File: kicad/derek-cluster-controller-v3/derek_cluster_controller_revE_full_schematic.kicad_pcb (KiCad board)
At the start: 6 copper layers, 220 x 220 mm, 59 parts, among them J1 XY301V_5.08_2P_5V_INPUT_15A, J2 FMHXG_RJ45NMCCFC_90D_RIGHT_AN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, J26 ADAFRUIT_815_PCA9685_BREAKOUT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, J3 FMHXG_RJ45NMCCFC_90D_RIGHT_AN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, J31 JST_XH_3PIN_PIR_LEFT, J32 JST_XH_3PIN_PIR_CENTER, J33 JST_XH_3PIN_PIR_RIGHT, J4 FMHXG_RJ45NMCCFC_90D_RIGHT_AN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, J40 TEST_POWER_3PIN, J41 TEST_I2C_4PIN, J42 TEST_LED_3PIN, J5 FMHXG_RJ45NMCCFC_90D_RIGHT_AN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, J51 DF1_SPEAKER_2PIN, J52 DF2_SPEAKER_2PIN, J6 FMHXG_RJ45NMCCFC_90D_RIGHT_AN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, J61 DF1_DAC_LR_GND_3PIN, J62 DF2_DAC_LR_GND_3PIN, J7 FMHXG_RJ45NMCCFC_90D_RIGHT_AN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, J8 FMHXG_RJ45NMCCFC_90D_RIGHT_AN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, J9 FMHXG_RJ45NMCCFC_90D_RIGHT_AN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, Q1 D2PAK_PMOS_REVERSE_PROTECTION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, SW1 DIP_SWITCH_4_SPST_2p54_CLUSTE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, U1 ESP32_S3_DEVKITC_1_SOCKET_2x1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, U3 DFPLAYER_MINI_STANDARD_20x20_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, U4 DFPLAYER_MINI_STANDARD_20x20_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, U5 SN74AHCT125N_DIP14_OR_SMD_LEV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

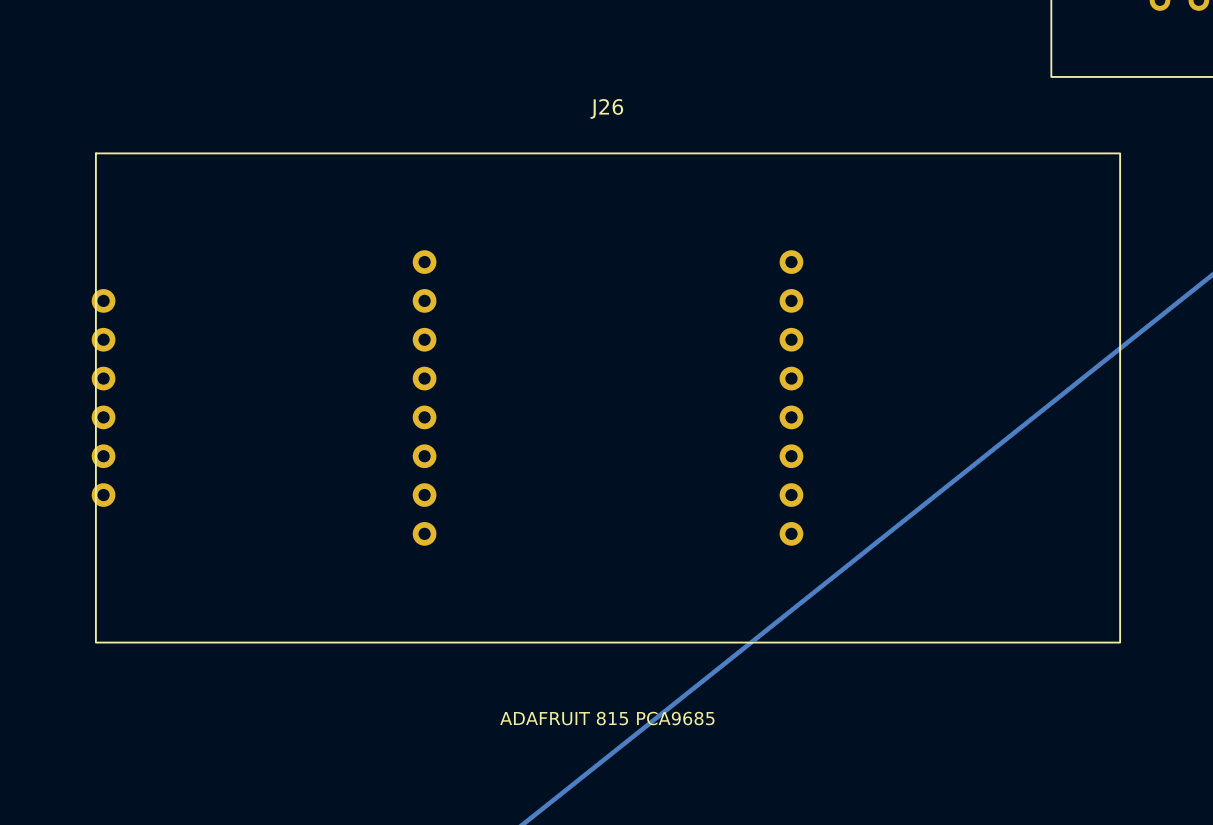
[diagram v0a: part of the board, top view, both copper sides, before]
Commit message: KiCad PCB files for cluster controller
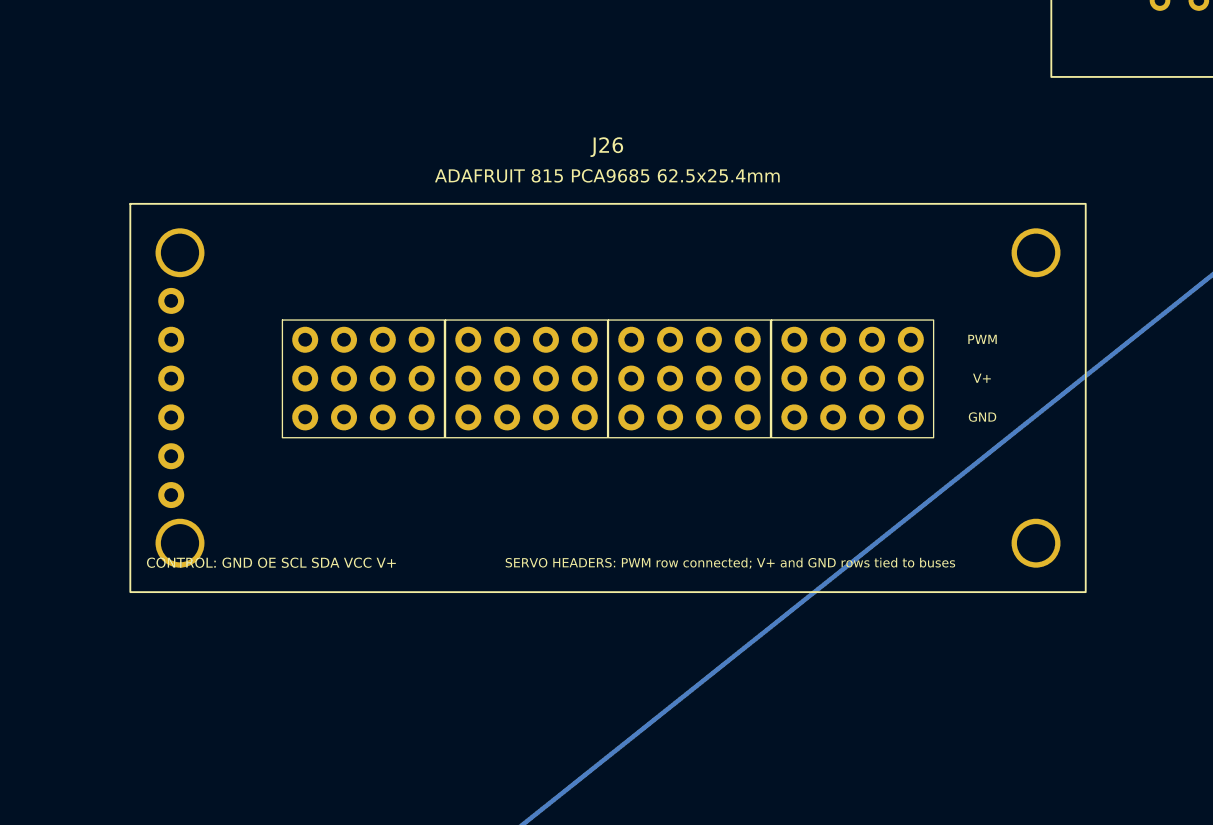
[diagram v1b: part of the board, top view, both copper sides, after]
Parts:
- J26: value ADAFRUIT_815_PCA9685_BREAKOUT_CARRIER_FOOTPRINT_VERIFY -> Adafruit Product 815 PCA9685 Breakout Socket; footprint ClusterActual:ADAFRUIT_815_PCA9685_BREAKOUT_CARRIER_FOOTPRINT_VERIFY -> ClusterActual:Adafruit_815_PCA9685_Breakout_CarrierSocket_VERIFY
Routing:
- net D4_LIFT: track 83.0 -> 103.3 mm
- net D4_PAN: track 85.1 -> 100.6 mm
- net D3_LIFT: track 91.8 -> 107.1 mm
- net D7_LIFT: track 101.2 -> 113.8 mm
- net D8_LIFT: track 111.9 -> 123.7 mm
- net D6_LIFT: track 96.3 -> 106.9 mm
- net D8_PAN: track 112.0 -> 122.4 mm
- net D7_PAN: track 102.0 -> 112.2 mm
- net D3_PAN: track 94.3 -> 104.2 mm
- net D2_LIFT: track 106.1 -> 114.0 mm
- net D6_PAN: track 97.7 -> 104.9 mm
- net D1_PAN: track 126.8 -> 121.0 mm
- net D5_LIFT: track 98.0 -> 103.2 mm
- net D2_PAN: track 108.8 -> 111.1 mm
- net D5_PAN: track 100.0 -> 100.9 mm

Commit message: minor tweak, still not right
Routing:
- net GND: vias 26 -> 25
- net 5V_PROT: vias 26 -> 27
